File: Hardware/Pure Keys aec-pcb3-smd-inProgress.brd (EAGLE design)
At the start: 158.7 x 51.7 mm, 72 parts, among them Q2 20MHz, U1 ATMEGA328P_TQFP

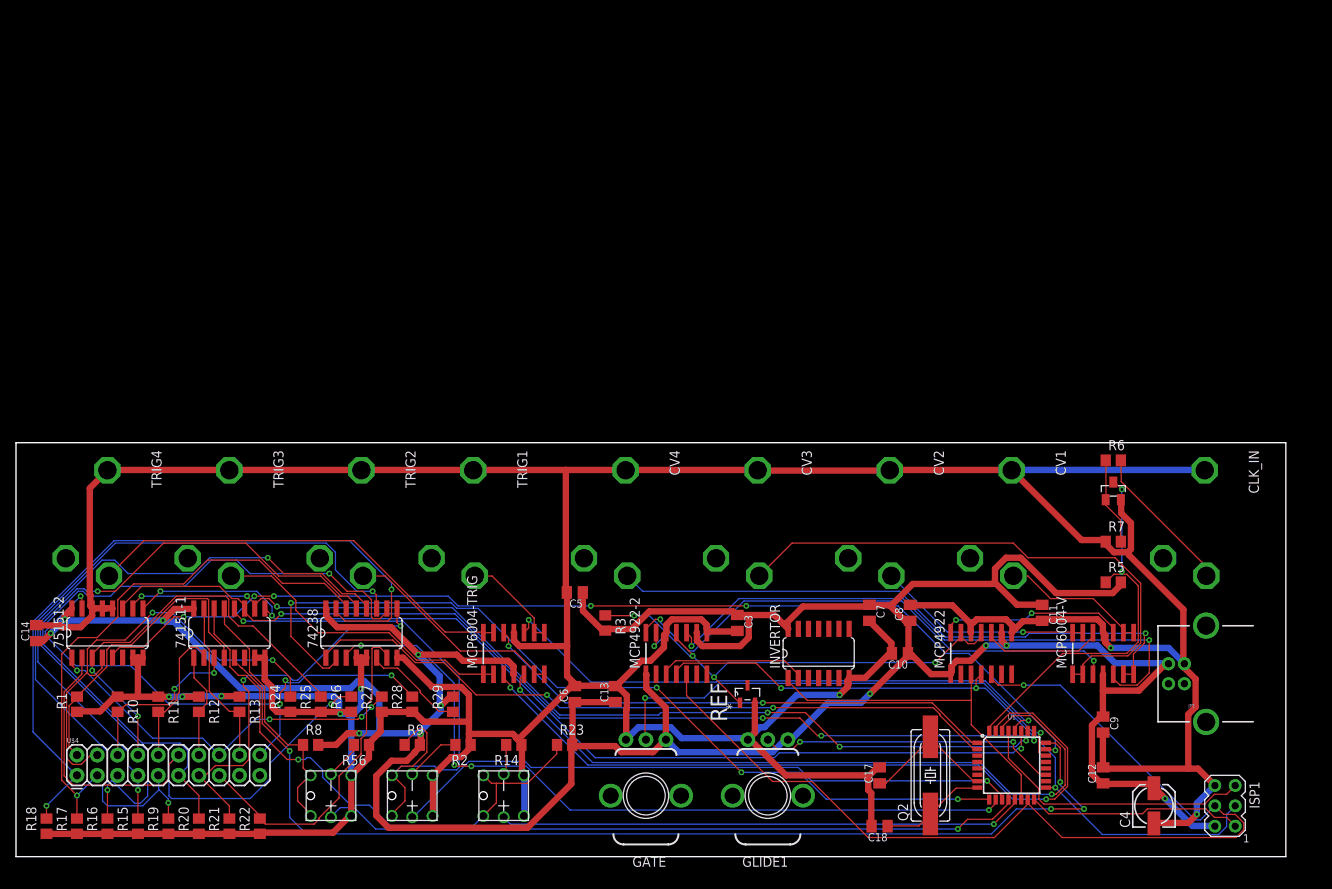
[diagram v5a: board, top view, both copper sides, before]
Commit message: Removed voltage class for SMD
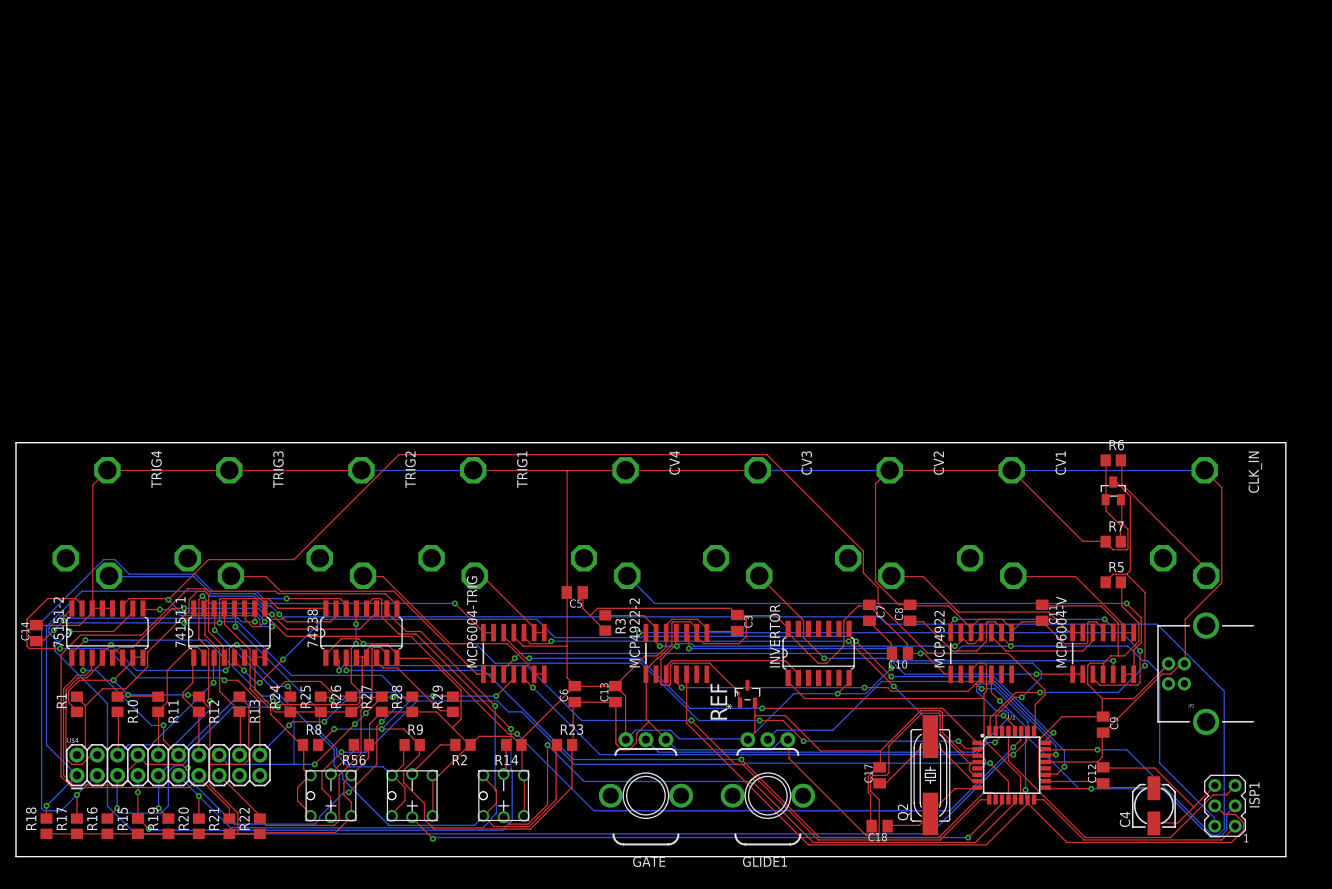
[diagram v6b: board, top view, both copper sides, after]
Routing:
- net 5V: track 414.7 -> 483.5 mm, vias 11 -> 10
- net GND: track 642.3 -> 709.3 mm, vias 8 -> 5
- net A1IN: track 123.9 -> 187.8 mm, vias 6 -> 3
- net DBIN: track 131.3 -> 190.6 mm, vias 6 -> 2
- net T6: track 49.9 -> 87.5 mm, vias 2 -> 0
- net A0IN: track 125.7 -> 162.0 mm, vias 4 -> 2
- net T4: track 92.7 -> 56.6 mm, vias 2 -> 4
- net BR1: track 53.2 -> 87.0 mm, vias 2 -> 4
- net T2: track 86.6 -> 57.7 mm, vias 2 -> 4
- net BUT2: track 70.9 -> 42.6 mm
- net TRIG2: track 91.4 -> 65.8 mm
- net T0: track 92.1 -> 68.0 mm
- net N$31: track 69.8 -> 46.8 mm, vias 0 -> 2
- net BR2: track 68.0 -> 45.8 mm, vias 1 -> 3
- net DAIN: track 135.2 -> 114.9 mm, vias 4 -> 6
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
